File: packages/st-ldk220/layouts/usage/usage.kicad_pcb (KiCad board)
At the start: 2 copper layers, 5 parts

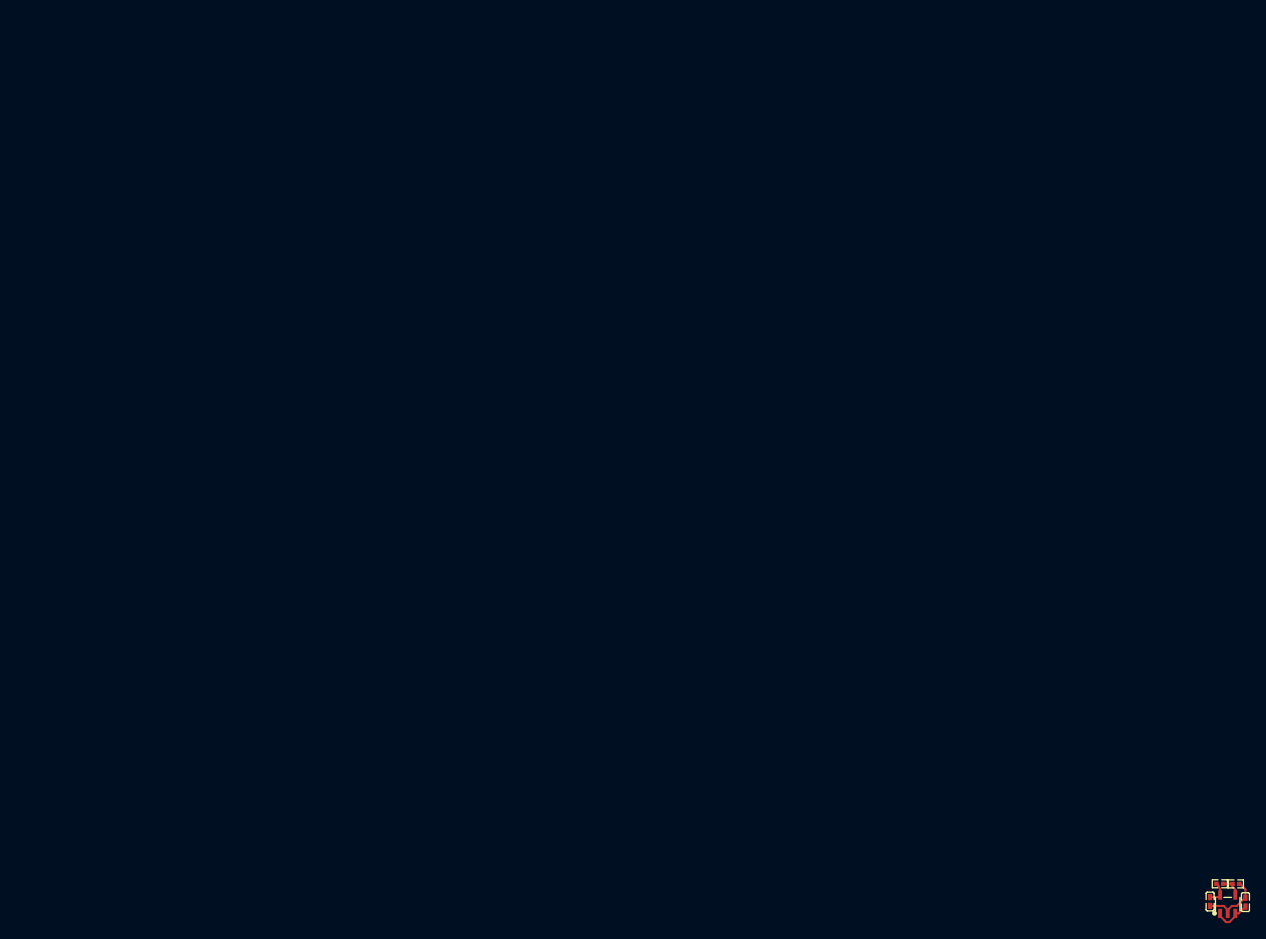
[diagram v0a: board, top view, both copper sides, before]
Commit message: Update picked parts and layouts for new voltage divider values
Generated by `ato build` after updating voltage divider API.

Co-Authored-By: Claude Opus 4.6 (1M context) <noreply@anthropic.com>
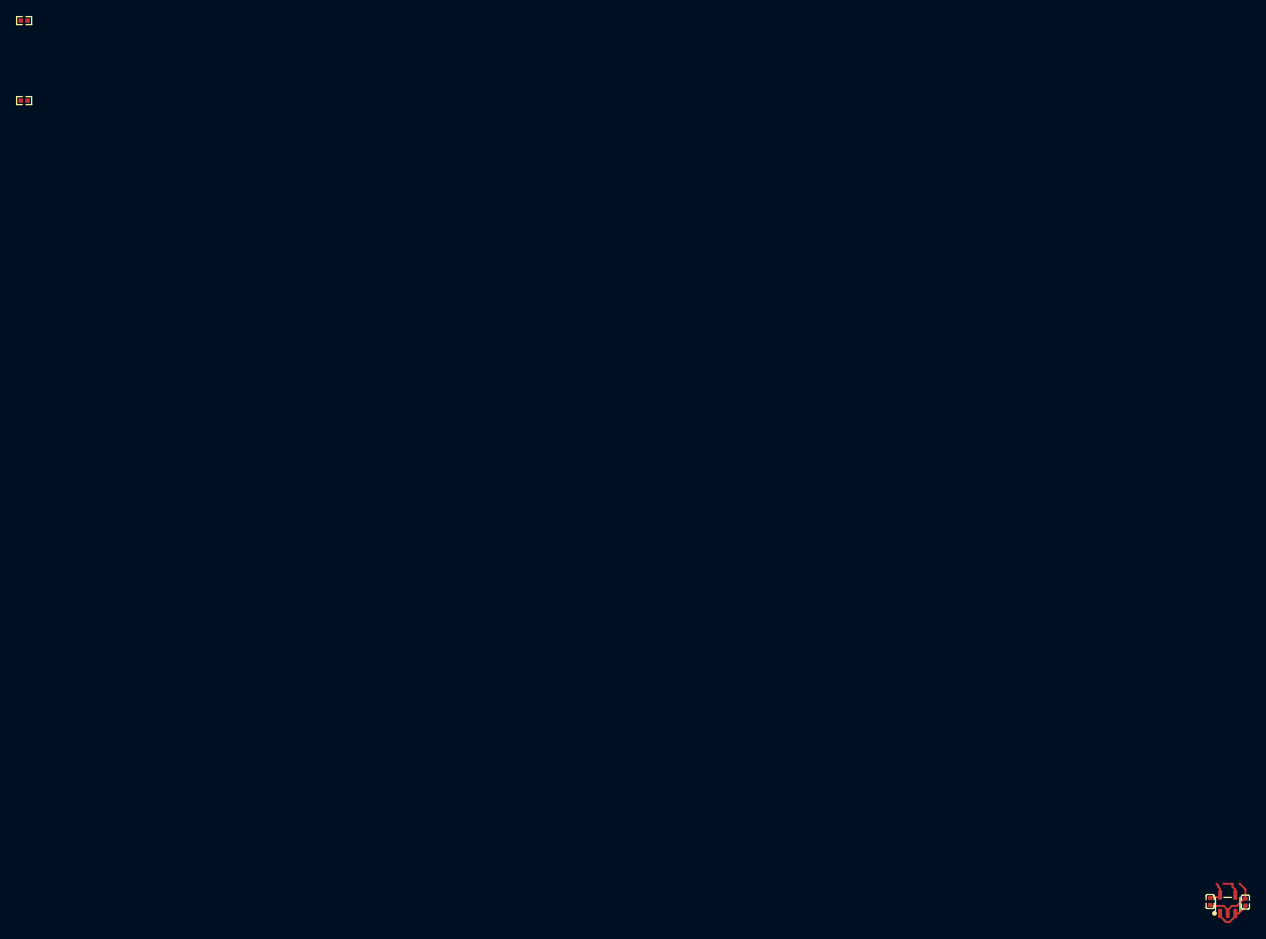
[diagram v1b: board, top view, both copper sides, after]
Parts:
- C1, C2: value 1µF ±10% 25V X5R -> 1µF ±10%
- R1: value 5.1kΩ ±1% 62.5mW -> 4.12kΩ ±1%; footprint UNI_ROYAL_0402WGF5101TCE:R0402 -> FOJAN_FRC0402F4121TS:R0402
- R2: value 10kΩ ±1% 62.5mW -> 2.37kΩ ±1%; footprint UNI_ROYAL_0402WGF1002TCE:R0402 -> UNI_ROYAL_0402WGF2371TCE:R0402
- moved R2 184.3 mm to (0.00, -10.0)
- moved R1 180.4 mm to (0.00, 0.00)
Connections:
- net power_in-VCC renamed power_in-hv
- C1 pad 2: GND -> power_in-lv
- C2 pad 1: power_shim-VCC -> hv
- C2 pad 2: GND -> lv
- R1 pad 1: VDIV_OUTPUT -> hv
- R1 pad 2: GND -> ref_out-hv
- R2 pad 1: power_shim-VCC -> ref_out-hv
- R2 pad 2: VDIV_OUTPUT -> lv
- U1 pad 2: GND -> power_in-lv
- U1 pad 4: VDIV_OUTPUT -> ref_out-hv
- U1 pad 5: power_shim-VCC -> hv
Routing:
- net power_in-lv: track 0.00 -> 8.20 mm
- net GND: track 8.20 -> 0.00 mm
- net (no net): track 0.00 -> 5.79 mm
- net power_shim-VCC: track 3.11 -> 0.00 mm
- net VDIV_OUTPUT: track 2.69 -> 0.00 mm

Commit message: Restore feedback divider resistor positions from pre-rename layouts
Copy the (at X Y angle) coordinates from the old r_top/r_bottom
footprints to the new chain.resistors[0]/chain.resistors[1] footprints
so board layouts are preserved.

Co-Authored-By: Claude Opus 4.6 (1M context) <noreply@anthropic.com>
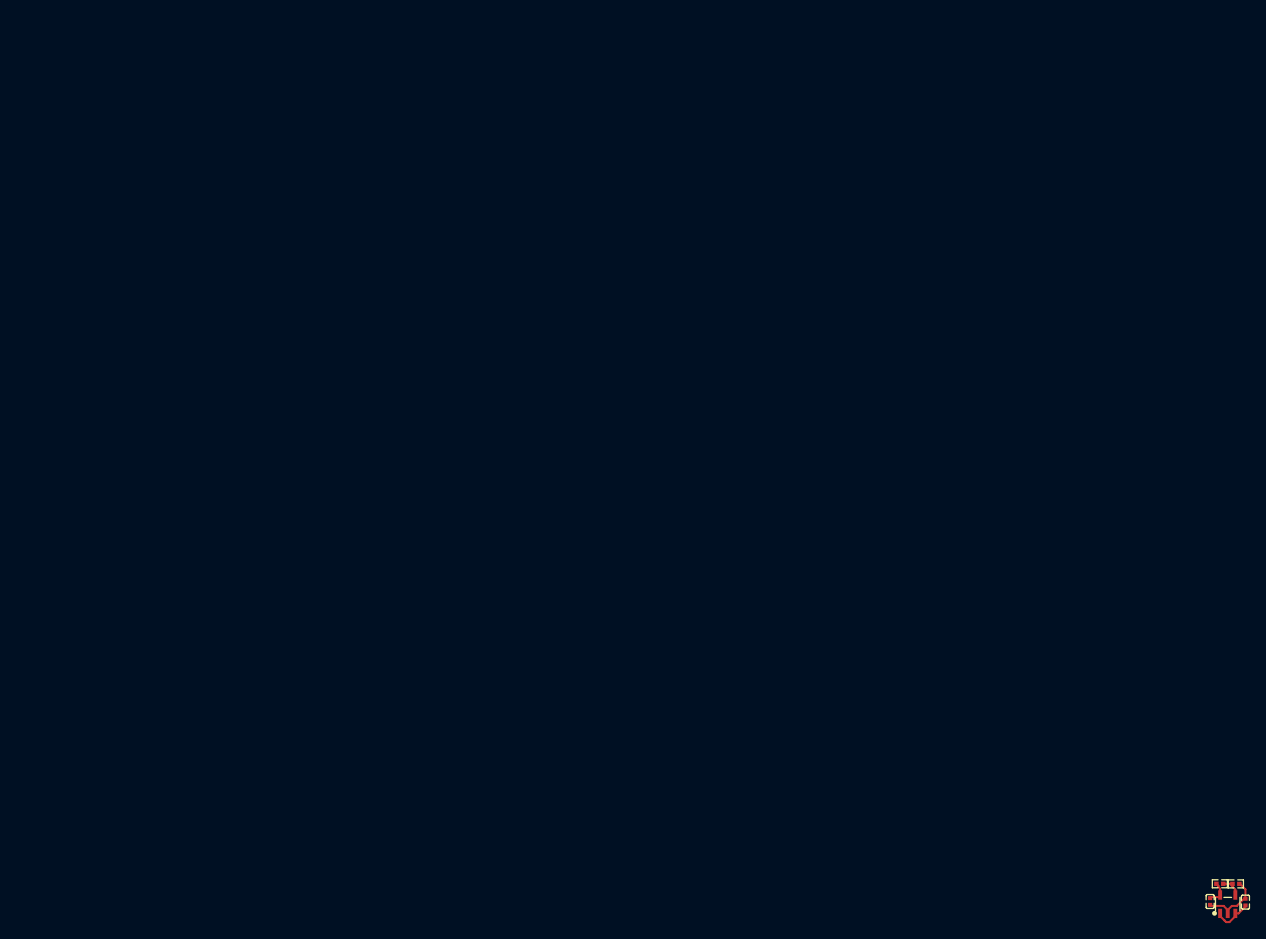
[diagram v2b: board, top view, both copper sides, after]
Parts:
- moved R2 186.0 mm to (151.5, 97.9)
- moved R1 178.7 mm to (149.5, 97.9)
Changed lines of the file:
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@@
 	(footprint "FOJAN_FRC0402F4121TS:R0402"
 		(layer "F.Cu")
-		(at 0 0 0)
+		(at 149.467116 97.898828 0)
 		(property "Reference" "R1"
 			(at -1.04 0 0)
@@
 	(footprint "UNI_ROYAL_0402WGF2371TCE:R0402"
 		(layer "F.Cu")
-		(at 0 -10 0)
+		(at 151.473894 97.91145 0)
 		(property "Reference" "R2"
 			(at -1.04 0 0)

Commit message: Regenerate parts and fix deprecated APIs for 8 packages
- Delete auto-picked resistors/capacitors across all 8 packages
- Regenerate IC, inductor, and diode parts with fresh checksums
  (fixes is_auto_generated checksum mismatch from pragma removal)
- Replace deprecated has_single_electric_reference_shared with
  has_single_electric_reference
- Rename gnd_only parameter to ground_only
- Fix _package suffix mismatches in ti-tps54560x imports
- Replace bridge connect operators with explicit pin connections
  for raw component parts in ti-tps54560x

Packages: ti-tps82130, ti-tpsm863257, ti-lv2842x, ti-tps563201,
ti-tps54560x, st-ldk220, ti-tlv75901, ti-tps63020

Co-Authored-By: Claude Opus 4.6 (1M context) <noreply@anthropic.com>
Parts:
- R1: value 4.12kΩ ±1% -> 2.61kΩ ±1%; footprint FOJAN_FRC0402F4121TS:R0402 -> UNI_ROYAL_0402WGF2611TCE:R0402
- R2: value 2.37kΩ ±1% -> 1.47kΩ ±1%; footprint UNI_ROYAL_0402WGF2371TCE:R0402 -> UNI_ROYAL_0402WGF1471TCE:R0402
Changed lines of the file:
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@@
 			)
 		)
-		(property "Datasheet" "https://lcsc.com/datasheet/lcsc_datasheet_1912202032_ST-LDK220M-R_C443854.pdf"
+		(property "Datasheet" "https://www.lcsc.com/datasheet/lcsc_datasheet_1912202032_STMicroelectronics-LDK220M-R_C443854.pdf"
 			(at 0 0 0)
 			(layer "User.9")
@@
 			)
 			(layer "F.SilkS")
+			(layers "F.SilkS")
+			(locked no)
 		)
 		(fp_line
@@
 			)
 			(layer "F.SilkS")
+			(layers "F.SilkS")
+			(locked no)
 		)
 		(fp_line
@@
 			)
 			(layer "F.SilkS")
+			(layers "F.SilkS")
+			(locked no)
 		)
 		(fp_circle
@@
 				(type solid)
 			)
-			(fill no)
-			(layer "F.SilkS")
+			(layer "F.SilkS")
+			(locked no)
 		)
 		(fp_circle
@@
 				(type solid)
 			)
-			(fill no)
 			(layer "Cmts.User")
+			(locked no)
 		)
 		(fp_circle
@@
 				(type solid)
 			)
-			(fill no)
 			(layer "F.Fab")
+			(locked no)
 		)
 		(pad "1" smd rect
@@
 			(net 6 "hv")
 		)
+		(embedded_fonts no)
 		(model "${KIPRJMOD}/../../parts/STMicroelectronics_LDK220M_R/SOT-23-5_L2.9-W1.6-H1.1-LS2.8-P0.95.step"
 			(offset
-				(xyz 0 0 0)
+				(xyz 0 0 -0)
 			)
 			(scale
@@
 		)
 	)
-	(footprint "FOJAN_FRC0402F4121TS:R0402"
+	(footprint "UNI_ROYAL_0402WGF2611TCE:R0402"
 		(layer "F.Cu")
 		(at 149.467116 97.898828 0)
@@
 			)
 		)
-		(property "Value" "4.12kΩ ±1%"
+		(property "Value" "2.61kΩ ±1%"
 			(at 0 4)
 			(layer "F.Fab")
@@
 			)
 		)
-		(property "LCSC" "C2930007"
-			(at 0 0 0)
-			(layer "User.9")
-			(hide yes)
-		)
-		(property "Manufacturer" "FOJAN"
+		(property "LCSC" "C34906"
+			(at 0 0 0)
+			(layer "User.9")
+			(hide yes)
+		)
+		(property "Manufacturer" "UNI-ROYAL(Uniroyal Elec)"
 			(at 0 0 0)
 			(layer "User.9")
@@
 			(hide yes)
 		)
-		(property "PARAM_resistance" "{\"type\": \"Quantity_Interval_Disjoint\", \"data\": {\"intervals\": {\"type\": \"Numeric_Interval_Disjoint\", \"data\": {\"intervals\": [{\"type\": \"Numeric_Interval\", \"data\": {\"min\": 4078.8000009208918, \"max\": 4161.199999079108}}]}}, \"unit\": \"ohm\"}}"
-			(at 0 0 0)
-			(layer "User.9")
-			(hide yes)
-		)
-		(property "Partnumber" "FRC0402F4121TS"
-			(at 0 0 0)
-			(layer "User.9")
-			(hide yes)
-		)
-		(property "Datasheet" "https://wmsc.lcsc.com/wmsc/upload/file/pdf/v2/lcsc/2308241009_FOJAN-FRC0402F4121TS_C2930007.pdf"
-			(at 0 0 0)
-			(layer "User.9")
-			(hide yes)
-		)
-		(property "resistance" "4.12kΩ ±1%"
+		(property "PARAM_resistance" "{\"type\": \"Quantity_Interval_Disjoint\", \"data\": {\"intervals\": {\"type\": \"Numeric_Interval_Disjoint\", \"data\": {\"intervals\": [{\"type\": \"Numeric_Interval\", \"data\": {\"min\": 2583.9000005833805, \"max\": 2636.0999994166195}}]}}, \"unit\": \"ohm\"}}"
+			(at 0 0 0)
+			(layer "User.9")
+			(hide yes)
+		)
+		(property "Partnumber" "0402WGF2611TCE"
+			(at 0 0 0)
+			(layer "User.9")
+			(hide yes)
+		)
+		(property "Datasheet" "https://www.lcsc.com/datasheet/lcsc_datasheet_2206010030_UNI-ROYAL-Uniroyal-Elec-0402WGF2611TCE_C34906.pdf"
+			(at 0 0 0)
+			(layer "User.9")
+			(hide yes)
+		)
+		(property "resistance" "2.61kΩ ±1%"
 			(at 0 0 0)
 			(layer "User.9")
@@
 			(hide yes)
 		)
-		(property "lcsc_id" "C2930007"
+		(property "lcsc_id" "C34906"
 			(at 0 0 0)
 			(layer "User.9")
@@
 			(hide yes)
 		)
-		(attr through_hole)
+		(attr smd)
 		(fp_line
 			(start -0.23 0.5)
@@
 		)
 		(embedded_fonts no)
-		(model "${KIPRJMOD}/../../parts/FOJAN_FRC0402F4121TS/R0402_L1.0-W0.5-H0.4.step"
+		(model "${KIPRJMOD}/../../parts/UNI_ROYAL_0402WGF2611TCE/R0402_L1.0-W0.5-H0.4.step"
 			(offset
-				(xyz 0 -0 0)
+				(xyz 0 0 -0)
 			)
 			(scale
@@
 		)
 	)
-	(footprint "UNI_ROYAL_0402WGF2371TCE:R0402"
+	(footprint "UNI_ROYAL_0402WGF1471TCE:R0402"
 		(layer "F.Cu")
 		(at 151.473894 97.91145 0)
@@
 			)
 		)
-		(property "Value" "2.37kΩ ±1%"
+		(property "Value" "1.47kΩ ±1%"
 			(at 0 4)
 			(layer "F.Fab")
@@
 			)
 		)
-		(property "LCSC" "C25881"
+		(property "LCSC" "C407715"
 			(at 0 0 0)
 			(layer "User.9")
@@
 			(hide yes)
 		)
-		(property "PARAM_resistance" "{\"type\": \"Quantity_Interval_Disjoint\", \"data\": {\"intervals\": {\"type\": \"Numeric_Interval_Disjoint\", \"data\": {\"intervals\": [{\"type\": \"Numeric_Interval\", \"data\": {\"min\": 2346.3000005297363, \"max\": 2393.6999994702637}}]}}, \"unit\": \"ohm\"}}"
-			(at 0 0 0)
-			(layer "User.9")
-			(hide yes)
-		)
-		(property "Partnumber" "0402WGF2371TCE"
-			(at 0 0 0)
-			(layer "User.9")
-			(hide yes)
-		)
-		(property "Datasheet" "https://www.lcsc.com/datasheet/lcsc_datasheet_2206010045_UNI-ROYAL-Uniroyal-Elec-0402WGF2371TCE_C25881.pdf"
-			(at 0 0 0)
-			(layer "User.9")
-			(hide yes)
-		)
-		(property "resistance" "2.37kΩ ±1%"
+		(property "PARAM_resistance" "{\"type\": \"Quantity_Interval_Disjoint\", \"data\": {\"intervals\": {\"type\": \"Numeric_Interval_Disjoint\", \"data\": {\"intervals\": [{\"type\": \"Numeric_Interval\", \"data\": {\"min\": 1455.3000003285706, \"max\": 1484.6999996714294}}]}}, \"unit\": \"ohm\"}}"
+			(at 0 0 0)
+			(layer "User.9")
+			(hide yes)
+		)
+		(property "Partnumber" "0402WGF1471TCE"
+			(at 0 0 0)
+			(layer "User.9")
+			(hide yes)
+		)
+		(property "Datasheet" "https://www.lcsc.com/datasheet/lcsc_datasheet_2205312000_UNI-ROYAL-Uniroyal-Elec-0402WGF1471TCE_C407715.pdf"
+			(at 0 0 0)
+			(layer "User.9")
+			(hide yes)
+		)
+		(property "resistance" "1.47kΩ ±1%"
 			(at 0 0 0)
 			(layer "User.9")
@@
 			(hide yes)
 		)
-		(property "lcsc_id" "C25881"
+		(property "lcsc_id" "C407715"
 			(at 0 0 0)
 			(layer "User.9")
@@
 		)
 		(embedded_fonts no)
-		(model "${KIPRJMOD}/../../parts/UNI_ROYAL_0402WGF2371TCE/R0402_L1.0-W0.5-H0.4.step"
+		(model "${KIPRJMOD}/../../parts/UNI_ROYAL_0402WGF1471TCE/R0402_L1.0-W0.5-H0.4.step"
 			(offset
 				(xyz 0 0 -0)
